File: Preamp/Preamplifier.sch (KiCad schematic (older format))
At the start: 168 parts, among them J1 Conn_01x02_Female, J10 AudioJack2, J11 Conn_01x05_Female, J12 XLR3, J13 Conn_01x03, J14 Conn_01x03, J15 Conn_01x02, J16 Conn_01x02, J17 Conn_01x02, J2 AudioJack2, J3 AudioJack3_SwitchTR, J4 AudioJack2_SwitchT, J5 AudioJack2_SwitchT, J6 Conn_01x02_Male, J7 Conn_01x02_Male, J8 Conn_01x05_Female, J9 AudioJack3_SwitchTR, Q1 2N3904, Q2 2N3906, Q3 2N3904, Q4 2N3906, Q5 BC549, SW1 SW_DPST, SW2 SW_SPDT, SW3 GND LIFT, SW4 SW_SPST, T1 Transformer_1P_2S, U1 OPA2134, U2 NE5532, U3 NE5532, U4 NE5532, U5 TL072, U6 NE5532, U7 NE5532, U8 NE5532, U9 NE5532

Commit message: Moved power supply off preamp
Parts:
- removed C1, C2: 1uF, Capacitor_THT:C_Rect_L7.2mm_W7.2mm_P5.00mm_FKS2_FKP2_MKS2_MKP2, symbol Device:C
- removed C10, C11, C17: 100uF 50V, Capacitor_THT:CP_Radial_D8.0mm_P3.50mm, symbol Device:CP
- removed C12, C13, C15, C16, C18, C19, C20, C21, C22, C23, C24, C25, C26, C27, C28, C30, C31, C33, C36, C37: 0.1uF, Capacitor_SMD:C_0805_2012Metric_Pad1.15x1.40mm_HandSolder, symbol Device:C
- removed C14: 100uF 50V, Capacitor_THT:CP_Radial_D8.0mm_P2.50mm, symbol Device:CP
- removed C29: 0.1uF (AUDIO), Capacitor_THT:C_Rect_L7.2mm_W2.5mm_P5.00mm_FKS2_FKP2_MKS2_MKP2, symbol Device:C
- removed C3, C6, C7, C9: 120n, Capacitor_THT:C_Rect_L7.2mm_W3.5mm_P5.00mm_FKS2_FKP2_MKS2_MKP2, symbol Device:C
- removed C32, C34, C35: 15nF, Capacitor_THT:C_Rect_L7.2mm_W2.5mm_P5.00mm_FKS2_FKP2_MKS2_MKP2, symbol Device:C
- removed C38, C39, C40, C8: 1000uF 50V, Capacitor_THT:CP_Radial_D17.0mm_P7.50mm, symbol Device:CP
- removed C4: 47uF 63V, Capacitor_THT:CP_Radial_D8.0mm_P5.00mm, symbol Device:CP
- removed C41, C42, C43, C44: 100uF 63V, Capacitor_THT:CP_Radial_D8.0mm_P3.50mm, symbol Device:CP
- removed C5: 10uF 50V, Capacitor_THT:CP_Radial_D6.3mm_P2.50mm, symbol Device:CP
- removed D1: D_Bridge_+-AA, symbol Device:D_Bridge_+-AA
- removed D10, D11, D2, D3, D4, D5, D6, D7: 1N4148, Diode_THT:D_DO-35_SOD27_P7.62mm_Horizontal, symbol Diode:1N4148
- removed D12: OVERLOAD, Connector_Phoenix_MSTB:PhoenixContact_MSTBA_2,5_2-G_1x02_P5.00mm_Horizontal, symbol Device:LED
- removed D13: POWER, Connector_Phoenix_MSTB:PhoenixContact_MSTBA_2,5_2-G-5,08_1x02_P5.08mm_Horizontal, symbol Device:LED
- removed D14, D15, D16, D17: 10V, Diode_THT:D_DO-41_SOD81_P7.62mm_Horizontal, symbol Device:D_Zener
- removed D8, D9: 1N5819, Diode_THT:D_DO-41_SOD81_P10.16mm_Horizontal, symbol Diode:1N5819
- removed F1: Fuse, Fuse:Fuseholder_Cylinder-5x20mm_Schurter_0031-8002_Horizontal_Open, symbol Device:Fuse
- removed F2, F3: Fuse, symbol Device:Fuse
- removed J1: Conn_01x02_Female, TerminalBlock_Dinkle:TerminalBlock_Dinkle_DT-55-B01X-02_P10.00mm, symbol Connector:Conn_01x02_Female
- removed J10, J2: AudioJack2, TerminalBlock_Phoenix:TerminalBlock_Phoenix_PT-1,5-2-3.5-H_1x02_P3.50mm_Horizontal, symbol Connector:AudioJack2
- removed J11, J8: Conn_01x05_Female, TerminalBlock_Phoenix:TerminalBlock_Phoenix_PT-1,5-5-3.5-H_1x05_P3.50mm_Horizontal, symbol Connector:Conn_01x05_Female
- removed J12: XLR3, TerminalBlock_Phoenix:TerminalBlock_Phoenix_PT-1,5-3-3.5-H_1x03_P3.50mm_Horizontal, symbol Connector:XLR3
- removed J13, J14: Conn_01x03, TerminalBlock_Phoenix:TerminalBlock_Phoenix_PT-1,5-3-3.5-H_1x03_P3.50mm_Horizontal, symbol Connector_Generic:Conn_01x03
- removed J15, J16, J17: Conn_01x02, TerminalBlock_Phoenix:TerminalBlock_Phoenix_PT-1,5-2-3.5-H_1x02_P3.50mm_Horizontal, symbol Connector_Generic:Conn_01x02
- removed J3, J9: AudioJack3_SwitchTR, TerminalBlock_Phoenix:TerminalBlock_Phoenix_PT-1,5-5-3.5-H_1x05_P3.50mm_Horizontal, symbol Connector:AudioJack3_SwitchTR
- removed J4, J5: AudioJack2_SwitchT, TerminalBlock_Phoenix:TerminalBlock_Phoenix_PT-1,5-3-3.5-H_1x03_P3.50mm_Horizontal, symbol Connector:AudioJack2_SwitchT
- removed J6, J7: Conn_01x02_Male, TerminalBlock_Phoenix:TerminalBlock_Phoenix_PT-1,5-2-5.0-H_1x02_P5.00mm_Horizontal, symbol Connector:Conn_01x02_Male
- removed Q1, Q3: 2N3904, Package_TO_SOT_THT:TO-92_Inline, symbol Transistor_BJT:2N3904
- removed Q2, Q4: 2N3906, Package_TO_SOT_THT:TO-92_Inline, symbol Transistor_BJT:2N3906
- removed Q5: BC549, Package_TO_SOT_THT:TO-92_Inline, symbol Transistor_BJT:BC549
- removed R1, R39: 1M, Resistor_SMD:R_0805_2012Metric_Pad1.15x1.40mm_HandSolder, symbol Device:R
- removed R10, R11, R20, R22, R3, R31, R32, R48, R5, R52, R6, R8, R9: 10k, Resistor_SMD:R_0805_2012Metric_Pad1.15x1.40mm_HandSolder, symbol Device:R
- removed R12: 0, Resistor_THT:R_Axial_DIN0207_L6.3mm_D2.5mm_P10.16mm_Horizontal, symbol Device:R
- removed R13, R17: 27k, Resistor_SMD:R_0805_2012Metric_Pad1.15x1.40mm_HandSolder, symbol Device:R
- removed R14: 100k, Resistor_SMD:R_0805_2012Metric_Pad1.15x1.40mm_HandSolder, symbol Device:R
- removed R15, R16, R35, R42: 22k, Resistor_SMD:R_0805_2012Metric_Pad1.15x1.40mm_HandSolder, symbol Device:R
- removed R18, R19, R23, R24, R38: 10K, Resistor_SMD:R_0805_2012Metric_Pad1.15x1.40mm_HandSolder, symbol Device:R
- removed R2: 560, Resistor_SMD:R_0805_2012Metric_Pad1.15x1.40mm_HandSolder, symbol Device:R
- removed R21: 1.8k, Resistor_SMD:R_0805_2012Metric_Pad1.15x1.40mm_HandSolder, symbol Device:R
- removed R25, R26, R27, R28: 3.9k, Resistor_SMD:R_0805_2012Metric_Pad1.15x1.40mm_HandSolder, symbol Device:R
- removed R29, R59, R60: 1k, Resistor_SMD:R_0805_2012Metric_Pad1.15x1.40mm_HandSolder, symbol Device:R
- removed R30, R33, R34: 100, Resistor_SMD:R_1206_3216Metric_Pad1.42x1.75mm_HandSolder, symbol Device:R
- removed R36: 12k, Resistor_SMD:R_0805_2012Metric_Pad1.15x1.40mm_HandSolder, symbol Device:R
- removed R37, R40, R41, R62, R63: 2.2K, Resistor_SMD:R_0805_2012Metric_Pad1.15x1.40mm_HandSolder, symbol Device:R
- removed R4: 2.7K, Resistor_SMD:R_0805_2012Metric_Pad1.15x1.40mm_HandSolder, symbol Device:R
- removed R43: 4.7k, Resistor_SMD:R_0805_2012Metric_Pad1.15x1.40mm_HandSolder, symbol Device:R
- removed R44, R45: 220, Resistor_SMD:R_1206_3216Metric_Pad1.42x1.75mm_HandSolder, symbol Device:R
- removed R46, R47, R50, R51: 5.6K, Resistor_SMD:R_0805_2012Metric_Pad1.15x1.40mm_HandSolder, symbol Device:R
- removed R49: 10 1W, Resistor_THT:R_Axial_DIN0411_L9.9mm_D3.6mm_P25.40mm_Horizontal, symbol Device:R
- removed R53, R55, R57: 6.8k, Resistor_SMD:R_0805_2012Metric_Pad1.15x1.40mm_HandSolder, symbol Device:R
- removed R54, R7: 1.8K, Resistor_SMD:R_0805_2012Metric_Pad1.15x1.40mm_HandSolder, symbol Device:R
- removed R56, R58: 6.8K, Resistor_SMD:R_0805_2012Metric_Pad1.15x1.40mm_HandSolder, symbol Device:R
- removed R61: 82k, Resistor_SMD:R_0805_2012Metric_Pad1.15x1.40mm_HandSolder, symbol Device:R
- removed RV1: 10K linear (gain), TerminalBlock_Phoenix:TerminalBlock_Phoenix_PT-1,5-6-3.5-H_1x06_P3.50mm_Horizontal, symbol Device:R_POT_Dual
- removed RV2: 1K log (headphone vol), TerminalBlock_Phoenix:TerminalBlock_Phoenix_PT-1,5-6-3.5-H_1x06_P3.50mm_Horizontal, symbol Device:R_POT_Dual
- removed RV3: 10k (SEND_LEVEL), TerminalBlock_Phoenix:TerminalBlock_Phoenix_PT-1,5-3-3.5-H_1x03_P3.50mm_Horizontal, symbol Device:R_POT
- removed RV4: 10k linear (FREQUENCY), TerminalBlock_Phoenix:TerminalBlock_Phoenix_PT-1,5-3-3.5-H_1x03_P3.50mm_Horizontal, symbol Device:R_POT
- removed RV5: 10k linear (BALANCE), TerminalBlock_Phoenix:TerminalBlock_Phoenix_PT-1,5-3-3.5-H_1x03_P3.50mm_Horizontal, symbol Device:R_POT
- removed SW1: SW_DPST, TerminalBlock_Phoenix:TerminalBlock_Phoenix_PT-1,5-4-3.5-H_1x04_P3.50mm_Horizontal, symbol Switch:SW_DPST
- removed SW2: SW_SPDT, TerminalBlock_Phoenix:TerminalBlock_Phoenix_PT-1,5-3-3.5-H_1x03_P3.50mm_Horizontal, symbol Switch:SW_SPDT
- removed SW3: GND LIFT, TerminalBlock_Phoenix:TerminalBlock_Phoenix_MKDS-3-2-5.08_1x02_P5.08mm_Horizontal, symbol Switch:SW_SPST
- removed SW4: SW_SPST, TerminalBlock_Phoenix:TerminalBlock_Phoenix_PT-1,5-2-3.5-H_1x02_P3.50mm_Horizontal, symbol Switch:SW_SPST
- removed T1: Transformer_1P_2S, Project-152-Bass-Guitar-Amp:TE 49008024RC62, symbol Device:Transformer_1P_2S
- removed U1: OPA2134, Package_DIP:DIP-8_W7.62mm_Socket, symbol Amplifier_Operational:TL072
- removed U2, U3, U4, U6, U7, U8, U9: NE5532, Package_DIP:DIP-8_W7.62mm_Socket, symbol Amplifier_Operational:NE5532
- removed U5: TL072, Package_DIP:DIP-8_W7.62mm_Socket, symbol Amplifier_Operational:TL072
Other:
- note removed: "(DNI C38 - extra if needed)"
- note removed: "(EQ board is separate)"
- note removed: "Crossover"
- note removed: "DI out"
- note removed: "EFX"
- note removed: "GAIN SW"
- note removed: "Gain Sw"
- note removed: "Headphone Amplifier"
- note removed: "Hi-pass filter Bypass\n"
- note removed: "High-pass filter to remove subsonic frequencies"
- note removed: "Initial Gain Stage"
- note removed: "Input for battery (connect to XT60 or similar)"
- note removed: "Input from MP3 player, etc."
- note removed: "OUTPUT CONN"
- note removed: "Output to headphones"
- note removed: "Overload indicator"
- note removed: "Power"
- note removed: "Power For Other Accessories"
- note removed: "Preamp power supply"
- note removed: "TE Connectivity 4900-8024RC62"
- note removed: "To Eq"
- note removed: "To the Power Amp"
- note removed: "Tuner Out"

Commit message: More layout
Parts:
- added C1, C2: 1uF, Capacitor_THT:C_Rect_L7.2mm_W7.2mm_P5.00mm_FKS2_FKP2_MKS2_MKP2, symbol Device:C
- added C10, C11: 100uF 50V, Capacitor_THT:CP_Radial_D8.0mm_P3.50mm, symbol Device:CP
- added C12, C13, C15, C16, C18, C19, C22, C23, C24, C25, C26, C27, C28, C30, C33, C36, C37: 0.1uF, Capacitor_SMD:C_0805_2012Metric_Pad1.15x1.40mm_HandSolder, symbol Device:C
- added C14: 100uF 50V, Capacitor_THT:CP_Radial_D8.0mm_P2.50mm, symbol Device:CP
- added C29: 0.1uF (AUDIO), Capacitor_THT:C_Rect_L7.2mm_W2.5mm_P5.00mm_FKS2_FKP2_MKS2_MKP2, symbol Device:C
- added C3, C6, C7, C9: 120n, Capacitor_THT:C_Rect_L7.2mm_W3.5mm_P5.00mm_FKS2_FKP2_MKS2_MKP2, symbol Device:C
- added C32, C34, C35: 15nF, Capacitor_THT:C_Rect_L7.2mm_W2.5mm_P5.00mm_FKS2_FKP2_MKS2_MKP2, symbol Device:C
- added C4: 47uF 63V, Capacitor_THT:CP_Radial_D8.0mm_P5.00mm, symbol Device:CP
- added C41, C42, C43, C44: 100uF 63V, Capacitor_THT:CP_Radial_D8.0mm_P3.50mm, symbol Device:CP
- added C5: 10uF 50V, Capacitor_THT:CP_Radial_D6.3mm_P2.50mm, symbol Device:CP
- added D10, D11, D2, D5, D6, D7: 1N4148, Diode_THT:D_DO-35_SOD27_P7.62mm_Horizontal, symbol Diode:1N4148
- added D12: OVERLOAD, LED_THT:LED_D3.0mm, symbol Device:LED
- added D13: POWER, LED_THT:LED_D3.0mm, symbol Device:LED
- added D14, D15, D16, D17: 10V, Diode_THT:D_DO-41_SOD81_P7.62mm_Horizontal, symbol Device:D_Zener
- added H1, H2, H3, H4: MountingHole, MountingHole:MountingHole_3.2mm_M3_ISO7380, symbol Mechanical:MountingHole
- added J1, J4, J5: Conn_01x03_Male, Connector_PinHeader_2.54mm:PinHeader_1x03_P2.54mm_Vertical, symbol Connector:Conn_01x03_Male
- added J12: XLR3, Connector_PinHeader_2.54mm:PinHeader_1x03_P2.54mm_Vertical, symbol Connector:XLR3
- added J14, J9: Conn_01x03, Connector_PinHeader_2.54mm:PinHeader_1x03_P2.54mm_Vertical, symbol Connector_Generic:Conn_01x03
- added J15, J16, J17: Conn_01x02, Connector_PinHeader_2.54mm:PinHeader_1x02_P2.54mm_Vertical, symbol Connector_Generic:Conn_01x02
- added J2, J3, J6: Conn_01x02_Male, Connector_PinHeader_2.54mm:PinHeader_1x02_P2.54mm_Vertical, symbol Connector:Conn_01x02_Male
- added J7: Conn_01x03, TerminalBlock_Phoenix:TerminalBlock_Phoenix_MKDS-1,5-3_1x03_P5.00mm_Horizontal, symbol Connector_Generic:Conn_01x03
- added J8: Conn_01x05_Female, Connector_PinHeader_2.54mm:PinHeader_1x05_P2.54mm_Vertical, symbol Connector:Conn_01x05_Female
- added Q3: 2N3904, Package_TO_SOT_THT:TO-92_Inline, symbol Transistor_BJT:2N3904
- added Q4: 2N3906, Package_TO_SOT_THT:TO-92_Inline, symbol Transistor_BJT:2N3906
- added Q5: BC549, Package_TO_SOT_THT:TO-92_Inline, symbol Transistor_BJT:BC549
- added R1, R39: 1M, Resistor_SMD:R_0805_2012Metric_Pad1.15x1.40mm_HandSolder, symbol Device:R
- added R10, R20, R22, R3, R32, R48, R5, R52, R6, R8, R9: 10k, Resistor_SMD:R_0805_2012Metric_Pad1.15x1.40mm_HandSolder, symbol Device:R
- added R11, R36: 12k, Resistor_SMD:R_0805_2012Metric_Pad1.15x1.40mm_HandSolder, symbol Device:R
- added R12, R64: 33k, Resistor_SMD:R_0805_2012Metric_Pad1.15x1.40mm_HandSolder, symbol Device:R
- added R13, R17: 27k, Resistor_SMD:R_0805_2012Metric_Pad1.15x1.40mm_HandSolder, symbol Device:R
- added R14: 100k, Resistor_SMD:R_0805_2012Metric_Pad1.15x1.40mm_HandSolder, symbol Device:R
- added R16, R35, R42: 22k, Resistor_SMD:R_0805_2012Metric_Pad1.15x1.40mm_HandSolder, symbol Device:R
- added R19, R24, R38: 10K, Resistor_SMD:R_0805_2012Metric_Pad1.15x1.40mm_HandSolder, symbol Device:R
- added R2: 560, Resistor_SMD:R_0805_2012Metric_Pad1.15x1.40mm_HandSolder, symbol Device:R
- added R21, R60: 1.8k, Resistor_SMD:R_0805_2012Metric_Pad1.15x1.40mm_HandSolder, symbol Device:R
- added R27, R28: 3.9k, Resistor_SMD:R_0805_2012Metric_Pad1.15x1.40mm_HandSolder, symbol Device:R
- added R29, R59: 1k, Resistor_SMD:R_0805_2012Metric_Pad1.15x1.40mm_HandSolder, symbol Device:R
- added R30, R33, R34: 100, Resistor_SMD:R_1206_3216Metric_Pad1.42x1.75mm_HandSolder, symbol Device:R
- added R37, R40, R41, R62, R63: 2.2K, Resistor_SMD:R_0805_2012Metric_Pad1.15x1.40mm_HandSolder, symbol Device:R
- added R4: 2.7K, Resistor_SMD:R_0805_2012Metric_Pad1.15x1.40mm_HandSolder, symbol Device:R
- added R43: 4.7k, Resistor_SMD:R_0805_2012Metric_Pad1.15x1.40mm_HandSolder, symbol Device:R
- added R44, R45: 220, Resistor_SMD:R_1206_3216Metric_Pad1.42x1.75mm_HandSolder, symbol Device:R
- added R46, R47, R50, R51: 5.6K, Resistor_SMD:R_0805_2012Metric_Pad1.15x1.40mm_HandSolder, symbol Device:R
- added R49: 10 1W, Resistor_THT:R_Axial_DIN0411_L9.9mm_D3.6mm_P12.70mm_Horizontal, symbol Device:R
- added R53, R55, R57: 6.8k, Resistor_SMD:R_0805_2012Metric_Pad1.15x1.40mm_HandSolder, symbol Device:R
- added R54, R7: 1.8K, Resistor_SMD:R_0805_2012Metric_Pad1.15x1.40mm_HandSolder, symbol Device:R
- added R56, R58: 6.8K, Resistor_SMD:R_0805_2012Metric_Pad1.15x1.40mm_HandSolder, symbol Device:R
- added R61, R65: 82k, Resistor_SMD:R_0805_2012Metric_Pad1.15x1.40mm_HandSolder, symbol Device:R
- added RV1: 10K linear (gain), Connector_PinHeader_2.54mm:PinHeader_1x06_P2.54mm_Vertical, symbol Device:R_POT_Dual
- added RV2: 10k log (headphone vol), Connector_PinHeader_2.54mm:PinHeader_1x03_P2.54mm_Vertical, symbol Device:R_POT
- added RV3: 10k (SEND_LEVEL), Connector_PinHeader_2.54mm:PinHeader_1x03_P2.54mm_Vertical, symbol Device:R_POT
- added RV4: 10k linear (FREQUENCY), Project-152-Bass-Guitar-Amp.pretty:RM-065-TRIMPOT, symbol Device:R_POT
- added RV5: 10k linear (BALANCE), Project-152-Bass-Guitar-Amp.pretty:RM-065-TRIMPOT, symbol Device:R_POT
- added SW1: SW_HPF, Connector_PinHeader_2.54mm:PinHeader_2x02_P2.54mm_Vertical, symbol Switch:SW_DPST
- added SW2: SW_SPDT, Connector_PinHeader_2.54mm:PinHeader_1x03_P2.54mm_Vertical, symbol Switch:SW_SPDT
- added SW3: GND LIFT, Connector_PinHeader_2.54mm:PinHeader_1x02_P2.54mm_Vertical, symbol Switch:SW_SPST
- added SW4: SW_SPST, Connector_PinHeader_2.54mm:PinHeader_1x02_P2.54mm_Vertical, symbol Switch:SW_SPST
- added SW5: SW_HPFQ, Connector_PinHeader_2.54mm:PinHeader_2x02_P2.54mm_Vertical, symbol Switch:SW_DPST
- added U1: OPA2134, Package_DIP:DIP-8_W7.62mm_Socket, symbol Amplifier_Operational:TL072
- added U2, U4, U6, U7, U8, U9: NE5532, Package_DIP:DIP-8_W7.62mm_Socket, symbol Amplifier_Operational:NE5532
- added U5: TL072, Package_DIP:DIP-8_W7.62mm_Socket, symbol Amplifier_Operational:TL072
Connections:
- new net: R4.1, R6.1, R7.1, U1.2 (-)
- new net: C4.1, R7.2
- new net: C4.2, R14.1, SW4.1 (A)
- new net: C5.2, D2.2 (A), RV1.1
- new net: R20.1, RV1.2, U1.5 (+)
- new net: C5.1, R6.2, U1.1
- new net: R2.1, U1.3 (+)
- new net: R21.1, R22.2, U1.6 (-)
- new net: C10.1, R22.1, U1.7
- new net: J2.2 (Pin_2), R1.2, R2.2
- new net: C7.2, R13.1, SW1.2, SW5.3, U2.1, U2.2 (-)
- new net: C6.1, R61.1, SW1.4, U2.3 (+)
- new net: C9.1, R65.1, SW1.1, U2.5 (+)
- new net: C11.1, R17.1, R64.1, U2.6 (-), U2.7
- new net: C3.1, C6.2, R12.2, R13.2
- new net: C2.1, R10.1
- new net: R10.2, R16.1, R8.2, R9.2, U4.2 (-)
- new net: C1.1, R9.1
- new net: D13.2 (A), R48.2
- new net: D12.2 (A), R43.2
- new net: C7.1, C9.2, R17.2, SW5.1
- new net: D10.2 (A), U5.1
- new net: R35.2, R36.1, U5.2 (-)
- new net: U5.6 (-), U5.7
- new net: C11.2, R30.2
- new net: C22.2, D10.1 (K), Q5.2 (B)
- new net: C14.1, Q3.1 (E), Q4.3 (C)
- new net: D5.2 (A), Q3.2 (B), R27.2
- new net: D6.1 (K), Q4.2 (B), R28.1
- new net: D5.1 (K), D6.2 (A), R24.2, U4.7
- new net: R19.2, R24.1, U4.6 (-)
- new net: R16.2, R19.1, U4.1
- new net: J5.3 (Pin_3), R33.1
- new net: R33.2, R34.2, RV2.2
- new net: J5.2 (Pin_2), R34.1
- new net: C14.2, R32.1, RV2.1
- new net: Q5.3 (E), R43.1
- new net: C2.2, J1.3 (Pin_3), R3.1
- new net: C1.2, J1.2 (Pin_2), R5.1
- new net: D11.2 (A), D14.2 (A), R41.1, R45.2, R62.2, U6.1
- new net: R40.2, R41.2, U6.2 (-)
- new net: R38.2, RV3.2, U6.3 (+)
- new net: R62.1, R63.2, U6.6 (-)
- new net: D16.2 (A), R44.2, R63.1, U6.7
- new net: C33.2, J12.1, R49.1
- new net: C44.1, J12.2
- new net: C43.1, J12.3
- new net: R49.2, SW3.2 (B)
- new net: RV3.1, SW2.2 (B)
- new net: R37.2, RV3.3
- new net: C41.1, R44.1
- new net: C42.1, R45.1
- new net: R64.2, SW5.2
- new net: R12.1, SW5.4
- new net: D16.1 (K), D17.1 (K)
- new net: R46.2, R47.1, U8.3 (+)
- new net: C29.1, R47.2, R58.2, U8.7
- new net: R50.1, R54.1, R56.2, U8.1
- new net: R50.2, R51.1, U8.2 (-)
- new net: D14.1 (K), D15.1 (K)
- new net: R54.2, RV4.3
- new net: C29.2, RV4.1, RV4.2, U8.6 (-)
- new net: C41.2, C43.2
- new net: C42.2, C44.2
- new net: C35.2, R57.1, U9.5 (+)
- new net: R52.1, R55.1, R59.1, U9.7
- new net: C32.2, C34.1, R52.2, R53.1
- new net: C34.2, C35.1, R55.2
- new net +12V: C12.2, C15.2, C18.2, C23.2, C25.2, C27.2, C30.2, C36.2, J7.1 (Pin_1), J8.2 (Pin_2), J9.1 (Pin_1), Q3.3 (C), Q5.1 (C), R27.1, R35.1, R48.1, U1.8 (V+), U2.8 (V+), U4.8 (V+), U5.8 (V+), U6.8 (V+), U7.8 (V+), U8.8 (V+), U9.8 (V+)
- new net -12V: C13.1, C16.1, C19.1, C24.1, C26.1, C28.1, C37.1, J7.3 (Pin_3), J8.3 (Pin_3), J9.3 (Pin_3), Q4.1 (E), R28.2, U1.4 (V-), U2.4 (V-), U4.4 (V-), U6.4 (V-), U7.4 (V-), U8.4 (V-), U9.4 (V-)
- new net EFXreturn: J4.3 (Pin_3), R42.2, R8.1, SW2.1 (A), U7.3 (+)
- new net EFXsend: J3.2 (Pin_2), J4.2 (Pin_2), R30.1
- new net FromEQ: C3.2, J8.5 (Pin_5), SW1.3
- new net GND: C12.1, C13.2, C15.1, C16.2, C18.1, C19.2, C23.1, C24.2, C25.1, C26.2, C27.1, C28.2, C33.1, C36.1, C37.2, D15.2 (A), D17.2 (A), J1.1 (Pin_1), J14.1 (Pin_1), J15.1 (Pin_1), J16.1 (Pin_1), J17.1 (Pin_1), J2.1 (Pin_1), J3.1 (Pin_1), J4.1 (Pin_1), J5.1 (Pin_1), J6.1 (Pin_1), J7.2 (Pin_2), J8.1 (Pin_1), J9.2 (Pin_2), R1.1, R11.2, R14.2, R20.2, R21.2, R3.2, R32.2, R37.1, R38.1, R4.2, R40.1, R42.1, R5.2, R51.2, R53.2, R57.2, R60.2, R61.2, R65.2, RV1.3, RV1.6, RV2.3, RV5.2, SW3.1 (A), SW4.2 (B), U4.3 (+), U4.5 (+), U6.5 (+), U8.5 (+)
- new net GNDD: C22.1, C30.1, D12.1 (K), D13.1 (K), R11.1, R36.2, R39.2, U5.4 (V-), U5.5 (+)
- new net HF: J14.2 (Pin_2), J15.2 (Pin_2), U9.1, U9.2 (-)
- new net HF*: R56.1, RV5.3, U9.3 (+)
- new net LF: J14.3 (Pin_3), J16.2 (Pin_2), U7.6 (-), U7.7
- new net LF*: R58.1, RV5.1, U7.5 (+)
- new net Overload: D11.1 (K), D2.1 (K), D7.1 (K), R39.1, U5.3 (+)
- new net PreEQ: C10.2, D7.2 (A), R29.2, RV1.4, SW2.3 (C)
- new net ToEQ: J8.4 (Pin_4), RV1.5
- new net Tuner: J6.2 (Pin_2), R29.1
- new net Tweeter: J17.2 (Pin_2), R59.2, R60.1, U9.6 (-)
- new net TweeterXOVR: C32.1, R46.1, U7.1, U7.2 (-)
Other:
- note added: "(EQ board is separate)"
- note added: "Crossover"
- note added: "DI out"
- note added: "EFX"
- note added: "Frequency Switch (27hz or 37hz)"
- note added: "GAIN SW"
- note added: "Gain Sw"
- note added: "Headphone Amplifier"
- note added: "Hi-pass filter Bypass\n"
- note added: "High-pass filter to remove subsonic frequencies"
- note added: "Initial Gain Stage"
- note added: "Input from MP3 player, etc."
- note added: "Output to headphones"
- note added: "Overload indicator"
- note added: "Power"
- note added: "Ring"
- note added: "Tip"
- note added: "Tip Switch"
- note added: "To 1/4" jack"
- note added: "To Eq"
- note added: "To the Power Amp"
- note added: "Tuner Out"

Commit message: More layout work
Still need to lay out the headphone amplifier.
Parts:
- removed J7: Conn_01x03, TerminalBlock_Phoenix:TerminalBlock_Phoenix_MKDS-1,5-3_1x03_P5.00mm_Horizontal, symbol Connector_Generic:Conn_01x03
- D2: footprint Diode_THT:D_DO-35_SOD27_P7.62mm_Horizontal -> Diode_SMD:D_SOD-123
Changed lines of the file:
@@
 F 0 "D2" V 5154 2779 50  0000 L CNN
 F 1 "1N4148" V 5245 2779 50  0000 L CNN
-F 2 "Diode_THT:D_DO-35_SOD27_P7.62mm_Horizontal" H 5200 2525 50  0001 C CNN
+F 2 "Diode_SMD:D_SOD-123" H 5200 2525 50  0001 C CNN
 F 3 "https://assets.nexperia.com/documents/data-sheet/1N4148_1N4448.pdf" H 5200 2700 50  0001 C CNN
 	1    5200 2700
@@
 Wire Wire Line
 	18300 14400 18850 14400
-$Comp
-L Connector_Generic:Conn_01x03 J7
-U 1 1 5F316C3C
-P 1750 1350
-F 0 "J7" H 1830 1392 50  0000 L CNN
-F 1 "Conn_01x03" H 1830 1301 50  0000 L CNN
-F 2 "TerminalBlock_Phoenix:TerminalBlock_Phoenix_MKDS-1,5-3_1x03_P5.00mm_Horizontal" H 1750 1350 50  0001 C CNN
-F 3 "~" H 1750 1350 50  0001 C CNN
-	1    1750 1350
-	1    0    0    -1
-$EndComp
-$Comp
-L power:+12V #PWR02
-U 1 1 5F3173A9
-P 1300 1150
-F 0 "#PWR02" H 1300 1000 50  0001 C CNN
-F 1 "+12V" H 1315 1323 50  0000 C CNN
-F 2 "" H 1300 1150 50  0001 C CNN
-F 3 "" H 1300 1150 50  0001 C CNN
-	1    1300 1150
-	1    0    0    -1
-$EndComp
-$Comp
-L power:-12V #PWR03
-U 1 1 5F317B5C
-P 1300 1600
-F 0 "#PWR03" H 1300 1700 50  0001 C CNN
-F 1 "-12V" H 1315 1773 50  0000 C CNN
-F 2 "" H 1300 1600 50  0001 C CNN
-F 3 "" H 1300 1600 50  0001 C CNN
-	1    1300 1600
-	-1   0    0    1
-$EndComp
-$Comp
-L power:GND #PWR01
-U 1 1 5F3186A1
-P 1050 1400
-F 0 "#PWR01" H 1050 1150 50  0001 C CNN
-F 1 "GND" H 1055 1227 50  0000 C CNN
-F 2 "" H 1050 1400 50  0001 C CNN
-F 3 "" H 1050 1400 50  0001 C CNN
-	1    1050 1400
-	1    0    0    -1
-$EndComp
-Wire Wire Line
-	1550 1350 1050 1350
-Wire Wire Line
-	1050 1350 1050 1400
-Wire Wire Line
-	1550 1250 1300 1250
-Wire Wire Line
-	1300 1250 1300 1150
-Wire Wire Line
-	1550 1450 1300 1450
-Wire Wire Line
-	1300 1450 1300 1600
 Text GLabel 12650 7850 0    50   Input ~ 0
 EFXreturn

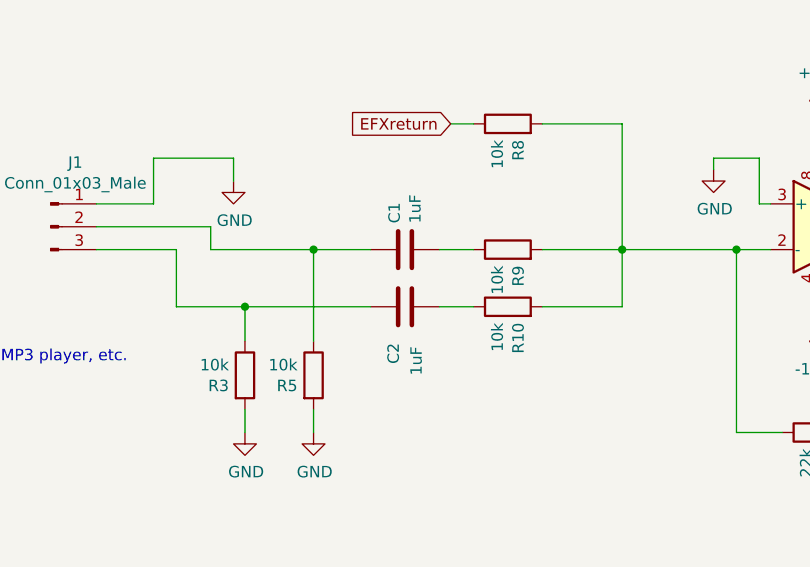
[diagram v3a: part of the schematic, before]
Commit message: Finished first pass at layout.
Still need to clean up silkscreen.
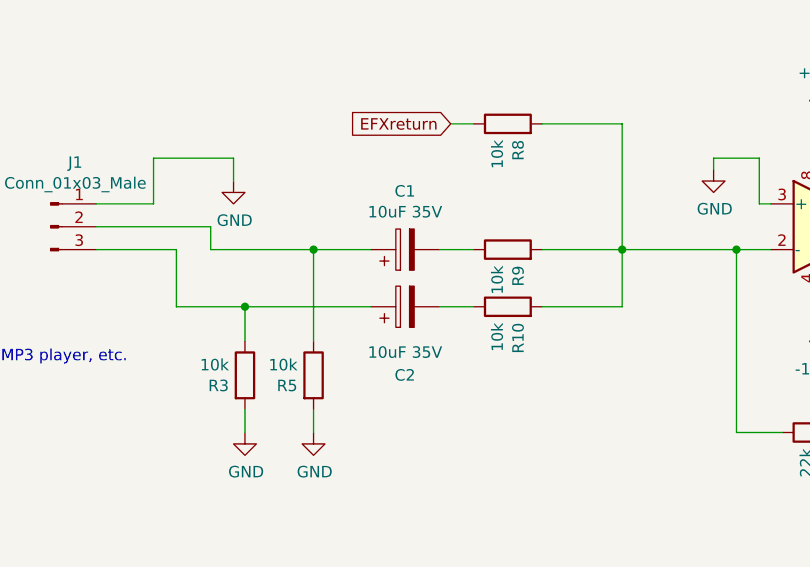
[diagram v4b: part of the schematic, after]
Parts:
- removed C1, C2: 1uF, Capacitor_THT:C_Rect_L7.2mm_W7.2mm_P5.00mm_FKS2_FKP2_MKS2_MKP2, symbol Device:C
- added C1, C2: 10uF 35V, Capacitor_THT:CP_Radial_D5.0mm_P2.00mm, symbol Device:CP
- D5, D6: footprint Diode_THT:D_DO-35_SOD27_P7.62mm_Horizontal -> Diode_SMD:D_SOD-123
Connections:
- net at R10.1: now also C2.2
- net at R9.1: now also C1.2
- net at J1.3 (Pin_3), R3.1: now also C2.1
- net at J1.2 (Pin_2), R5.1: now also C1.1
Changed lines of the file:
@@
 Wire Wire Line
 	2650 13500 2650 13600
-$Comp
-L Device:C C1
-U 1 1 5D8C8029
-P 3350 12800
-F 0 "C1" H 3235 12754 50  0000 R CNN
-F 1 "1uF" H 3235 12845 50  0000 R CNN
-F 2 "Capacitor_THT:C_Rect_L7.2mm_W7.2mm_P5.00mm_FKS2_FKP2_MKS2_MKP2" H 3388 12650 50  0001 C CNN
-F 3 "~" H 3350 12800 50  0001 C CNN
-	1    3350 12800
-	0    1    1    0
-$EndComp
 Wire Wire Line
 	2000 12600 2250 12600
@@
 	2950 12800 2500 12800
 $Comp
-L Device:C C2
-U 1 1 5D8E413A
-P 3350 13050
-F 0 "C2" H 3600 13000 50  0000 R CNN
-F 1 "1uF" H 3650 13100 50  0000 R CNN
-F 2 "Capacitor_THT:C_Rect_L7.2mm_W7.2mm_P5.00mm_FKS2_FKP2_MKS2_MKP2" H 3388 12900 50  0001 C CNN
-F 3 "~" H 3350 13050 50  0001 C CNN
-	1    3350 13050
-	0    1    1    0
-$EndComp
-$Comp
 L Device:R R10
 U 1 1 5D7274BA
@@
 F 0 "D5" V 7846 12371 50  0000 R CNN
 F 1 "1N4148" V 7755 12371 50  0000 R CNN
-F 2 "Diode_THT:D_DO-35_SOD27_P7.62mm_Horizontal" H 7800 12275 50  0001 C CNN
+F 2 "Diode_SMD:D_SOD-123" H 7800 12275 50  0001 C CNN
 F 3 "https://assets.nexperia.com/documents/data-sheet/1N4148_1N4448.pdf" H 7800 12450 50  0001 C CNN
 	1    7800 12450
@@
 F 0 "D6" V 7846 12671 50  0000 R CNN
 F 1 "1N4148" V 7755 12671 50  0000 R CNN
-F 2 "Diode_THT:D_DO-35_SOD27_P7.62mm_Horizontal" H 7800 12575 50  0001 C CNN
+F 2 "Diode_SMD:D_SOD-123" H 7800 12575 50  0001 C CNN
 F 3 "https://assets.nexperia.com/documents/data-sheet/1N4148_1N4448.pdf" H 7800 12750 50  0001 C CNN
 	1    7800 12750
@@
 	1    0    0    -1
 $EndComp
+$Comp
+L Device:CP C2
+U 1 1 5E5613E5
+P 3350 13050
+F 0 "C2" V 3050 13050 50  0000 C CNN
+F 1 "10uF 35V" V 3150 13050 50  0000 C CNN
+F 2 "Capacitor_THT:CP_Radial_D5.0mm_P2.00mm" H 3388 12900 50  0001 C CNN
+F 3 "~" H 3350 13050 50  0001 C CNN
+	1    3350 13050
+	0    -1   -1   0
+$EndComp
+$Comp
+L Device:CP C1
+U 1 1 5E562091
+P 3350 12800
+F 0 "C1" V 3605 12800 50  0000 C CNN
+F 1 "10uF 35V" V 3514 12800 50  0000 C CNN
+F 2 "Capacitor_THT:CP_Radial_D5.0mm_P2.00mm" H 3388 12650 50  0001 C CNN
+F 3 "~" H 3350 12800 50  0001 C CNN
+	1    3350 12800
+	0    -1   -1   0
+$EndComp
 $EndSCHEMATC

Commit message: Added overload connector for EQ
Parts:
- added J7: Conn_01x02, Connector_PinHeader_2.54mm:PinHeader_1x02_P2.54mm_Vertical, symbol Connector_Generic:Conn_01x02
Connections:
- net GND: now also J7.1 (Pin_1)
- net Overload: now also J7.2 (Pin_2)
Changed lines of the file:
@@
 	0    -1   -1   0
 $EndComp
+$Comp
+L Connector_Generic:Conn_01x02 J7
+U 1 1 5E4DCB7D
+P 8950 11250
+F 0 "J7" H 9030 11242 50  0000 L CNN
+F 1 "Conn_01x02" H 9030 11151 50  0000 L CNN
+F 2 "Connector_PinHeader_2.54mm:PinHeader_1x02_P2.54mm_Vertical" H 8950 11250 50  0001 C CNN
+F 3 "~" H 8950 11250 50  0001 C CNN
+	1    8950 11250
+	1    0    0    -1
+$EndComp
+Text GLabel 8750 11350 0    50   Input ~ 0
+Overload
+$Comp
+L power:GND #PWR01
+U 1 1 5E4E06DC
+P 8200 11200
+F 0 "#PWR01" H 8200 10950 50  0001 C CNN
+F 1 "GND" H 8205 11027 50  0000 C CNN
+F 2 "" H 8200 11200 50  0001 C CNN
+F 3 "" H 8200 11200 50  0001 C CNN
+	1    8200 11200
+	1    0    0    -1
+$EndComp
+Wire Wire Line
+	8750 11250 8500 11250
+Wire Wire Line
+	8500 11250 8500 11200
+Wire Wire Line
+	8500 11200 8200 11200
 $EndSCHEMATC
